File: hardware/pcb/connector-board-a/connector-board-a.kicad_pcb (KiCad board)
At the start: 2 copper layers, 27.4 x 39.1 mm, 22 parts, among them J1 DE9_Pins, J2 8-215570-0, Q3 2N7002, U4 TPS63001

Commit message: Routing of connector b board
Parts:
- J2: footprint TwinOak platform footprints:82155700 -> TwinOak:82155700
- JP1: value PWM -> PWM_MODE; footprint Jumper:SolderJumper-2_P1.3mm_Open_RoundedPad1.0x1.5mm -> Connector_PinHeader_2.54mm:PinHeader_1x02_P2.54mm_Vertical
- moved JP1 1.19 mm to (133.1, 107.2), turned to -90 degrees
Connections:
- net Net-(U4-PS/SYNC) renamed PS_SYNC
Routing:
- net I2C_SCL: track 26.7 -> 28.6 mm
- net VBAT_RAW: track 85.7 -> 87.3 mm, vias 2 -> 1
- net I2C_SDA: track 21.0 -> 21.8 mm
- net PS_SYNC: track 5.04 -> 5.76 mm

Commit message: Cleanup. Added feedback prevention circuits to Walter adapter
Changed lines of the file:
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@@
 		(pad "1" thru_hole rect
 			(at 0 0 180)
-			(size 1.3 1.3)
+			(size 1.3 1.8)
 			(drill 0.8)
 			(layers "*.Cu" "*.Mask")
@@
 			(pintype "passive")
 		)
-		(pad "2" thru_hole circle
+		(pad "2" thru_hole oval
 			(at 1.27 2.54 180)
-			(size 1.3 1.3)
+			(size 1.3 1.8)
 			(drill 0.8)
 			(layers "*.Cu" "*.Mask")
@@
 			(pinfunction "2_2")
 			(pintype "passive")
+			(thermal_bridge_angle 45)
 		)
 		(pad "3" thru_hole oval
 			(at 2.54 0 180)
-			(size 1.3 1.3)
+			(size 1.3 1.8)
 			(drill 0.8)
 			(layers "*.Cu" "*.Mask")
@@
 			(thermal_bridge_angle 45)
 		)
-		(pad "4" thru_hole circle
+		(pad "4" thru_hole oval
 			(at 3.81 2.54 180)
-			(size 1.3 1.3)
+			(size 1.3 1.8)
 			(drill 0.8)
 			(layers "*.Cu" "*.Mask")
@@
 			(pinfunction "4_4")
 			(pintype "passive")
+			(thermal_bridge_angle 45)
 		)
-		(pad "5" thru_hole circle
+		(pad "5" thru_hole oval
 			(at 5.08 0 180)
-			(size 1.3 1.3)
+			(size 1.3 1.8)
 			(drill 0.8)
 			(layers "*.Cu" "*.Mask")
@@
 			(pinfunction "5_5")
 			(pintype "passive")
+			(thermal_bridge_angle 45)
 		)
-		(pad "6" thru_hole circle
+		(pad "6" thru_hole oval
 			(at 6.35 2.54 180)
-			(size 1.3 1.3)
+			(size 1.3 1.8)
 			(drill 0.8)
 			(layers "*.Cu" "*.Mask")
@@
 			(pinfunction "6_6")
 			(pintype "passive")
+			(thermal_bridge_angle 45)
 		)
-		(pad "7" thru_hole circle
+		(pad "7" thru_hole oval
 			(at 7.62 0 180)
-			(size 1.3 1.3)
+			(size 1.3 1.8)
 			(drill 0.8)
 			(layers "*.Cu" "*.Mask")
@@
 			(pinfunction "7_7")
 			(pintype "passive")
+			(thermal_bridge_angle 45)
 		)
-		(pad "8" thru_hole circle
+		(pad "8" thru_hole oval
 			(at 8.89 2.54 180)
-			(size 1.3 1.3)
+			(size 1.3 1.8)
 			(drill 0.8)
 			(layers "*.Cu" "*.Mask")
@@
 			(pinfunction "8_8")
 			(pintype "passive")
+			(thermal_bridge_angle 45)
 		)
-		(pad "9" thru_hole circle
+		(pad "9" thru_hole oval
 			(at 10.16 0 180)
-			(size 1.3 1.3)
+			(size 1.3 1.8)
 			(drill 0.8)
 			(layers "*.Cu" "*.Mask")
@@
 			(pinfunction "9_9")
 			(pintype "passive")
+			(thermal_bridge_angle 45)
 		)
-		(pad "10" thru_hole circle
+		(pad "10" thru_hole oval
 			(at 11.43 2.54 180)
-			(size 1.3 1.3)
+			(size 1.3 1.8)
 			(drill 0.8)
 			(layers "*.Cu" "*.Mask")
@@
 			(pinfunction "10_10")
 			(pintype "passive")
+			(thermal_bridge_angle 45)
 		)
 		(embedded_fonts no)
@@
 		(start 131.572 98.806)
 		(end 130.328 97.562)
-		(width 0.254)
+		(width 0.508)
 		(layer "F.Cu")
 		(net "Net-(U4-L1)")
@@
 		(start 132.58 98.814)
 		(end 133.858 97.536)
-		(width 0.254)
+		(width 0.508)
 		(layer "F.Cu")
 		(net "Net-(U4-L2)")
@@
 	)
 	(segment
-		(start 143.866 100.228)
-		(end 143.256 100.838)
-		(width 0.254)
-		(layer "B.Cu")
-		(net "GND")
-	)
-	(segment
 		(start 134.112 85.344)
 		(end 132.334 85.344)
@@
 	)
 	(segment
-		(start 133.604 92.964)
-		(end 133.35 93.218)
+		(start 143.002 100.838)
+		(end 132.08 100.838)
 		(width 0.254)
 		(layer "B.Cu")
@@
 	)
 	(segment
-		(start 145.184 100.228)
-		(end 143.866 100.228)
+		(start 133.604 92.964)
+		(end 133.35 93.218)
 		(width 0.254)
 		(layer "B.Cu")
@@
 	)
 	(segment
-		(start 133.604 91.44)
-		(end 133.604 92.964)
+		(start 143.612 100.228)
+		(end 143.002 100.838)
 		(width 0.254)
 		(layer "B.Cu")
@@
 	)
 	(segment
-		(start 134.112 85.344)
-		(end 134.112 75.692)
+		(start 133.604 91.44)
+		(end 133.604 92.964)
 		(width 0.254)
 		(layer "B.Cu")
@@
 	)
 	(segment
-		(start 143.256 100.838)
-		(end 132.08 100.838)
+		(start 134.112 85.344)
+		(end 134.112 75.692)
 		(width 0.254)
 		(layer "B.Cu")
@@
 	)
 	(segment
+		(start 145.184 100.228)
+		(end 143.612 100.228)
+		(width 0.254)
+		(layer "B.Cu")
+		(net "GND")
+	)
+	(segment
 		(start 137.549 72.255)
 		(end 149.217 72.255)
@@
 		(start 131.196 91.44)
 		(end 131.196 93.122)
-		(width 0.254)
+		(width 0.508)
 		(layer "F.Cu")
 		(net "VBAT_RAW")
@@
 		(start 129.032 93.98)
 		(end 129.032 99.822)
-		(width 0.254)
+		(width 0.508)
 		(layer "F.Cu")
 		(net "VBAT_RAW")
@@
 		(start 131.292 93.218)
 		(end 129.794 93.218)
-		(width 0.254)
+		(width 0.508)
 		(layer "F.Cu")
 		(net "VBAT_RAW")
@@
 		(start 129.416 99.438)
 		(end 131.08 99.438)
-		(width 0.254)
+		(width 0.508)
 		(layer "F.Cu")
 		(net "VBAT_RAW")
@@
 		(start 129.794 93.218)
 		(end 129.032 93.98)
-		(width 0.254)
+		(width 0.508)
 		(layer "F.Cu")
 		(net "VBAT_RAW")
@@
 		(start 129.032 99.822)
 		(end 129.416 99.438)
-		(width 0.254)
+		(width 0.508)
 		(layer "F.Cu")
 		(net "VBAT_RAW")
@@
 		(start 129.032 104.648)
 		(end 129.032 99.314)
-		(width 0.254)
+		(width 0.508)
 		(layer "B.Cu")
 		(net "VBAT_RAW")
@@
 		(start 133.101 107.188)
 		(end 133.101 105.669)
-		(width 0.254)
+		(width 0.508)
 		(layer "B.Cu")
 		(net "VBAT_RAW")
@@
 		(start 132.588 105.156)
 		(end 129.54 105.156)
-		(width 0.254)
+		(width 0.508)
 		(layer "B.Cu")
 		(net "VBAT_RAW")
@@
 		(start 129.54 105.156)
 		(end 129.032 104.648)
-		(width 0.254)
+		(width 0.508)
 		(layer "B.Cu")
 		(net "VBAT_RAW")
@@
 		(start 133.101 105.669)
 		(end 132.588 105.156)
-		(width 0.254)
+		(width 0.508)
 		(layer "B.Cu")
 		(net "VBAT_RAW")

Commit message: Final PCB adjuments to rev 1.1
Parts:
- moved C16 7.92 mm to (127.0, 97.5), turned to 90 degrees
- moved C17 5.43 mm to (128.8, 97.5), turned to 90 degrees
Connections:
- J1 pad SH: (no net) -> GND
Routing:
- net GND: track 83.4 -> 93.5 mm, vias 12 -> 42
- net VBAT_RAW: track 87.3 -> 79.9 mm
- net Net-(Q3-D): track 17.5 -> 18.0 mm, vias 0 -> 2
- added copper zone on F.Cu, net GND

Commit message: Routed new BME280 addition to connector A
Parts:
- added C22: 100n, Capacitor_SMD:C_0603_1608Metric, F.Cu at (127.3, 77.2)
- added C23: 100n, Capacitor_SMD:C_0603_1608Metric, F.Cu at (128.0, 74.9)
- added J3: J_ENV, Connector_PinHeader_2.54mm:PinHeader_1x04_P2.54mm_Vertical, F.Cu at (128.0, 81.3)
- added U5: BME280, Package_LGA:Bosch_LGA-8_2.5x2.5mm_P0.65mm_ClockwisePinNumbering, F.Cu at (130.1, 77.5)
- moved Q3 1.97 mm to (129.0, 88.9)
- moved R13 1.97 mm to (134.3, 88.7)
- moved C18 1.97 mm to (132.3, 88.8)
- moved R12 1.95 mm to (134.4, 84.8)
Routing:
- net 3V3_LORA: track 25.1 -> 63.0 mm
- net GND: track 93.5 -> 68.6 mm, vias 42 -> 44
- net I2C_SDA: track 21.8 -> 44.7 mm, vias 0 -> 1
- net I2C_SCL: track 28.6 -> 38.2 mm, vias 0 -> 1
- net Net-(Q3-D): track 18.0 -> 16.1 mm
- net LORA_PWR_KILL: track 17.4 -> 19.3 mm
- net Net-(Q3-G): track 10.7 -> 9.13 mm

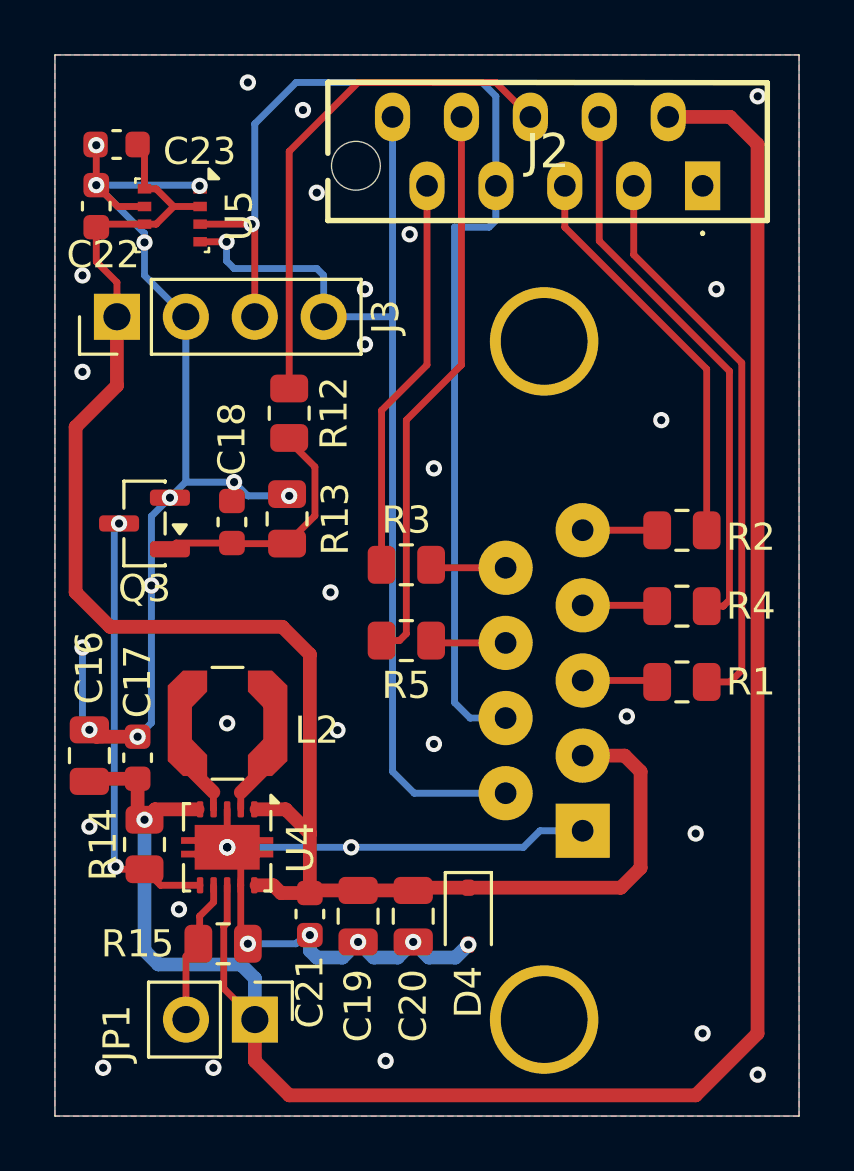
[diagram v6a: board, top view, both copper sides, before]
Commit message: Changed via placements to avoid solderwicking
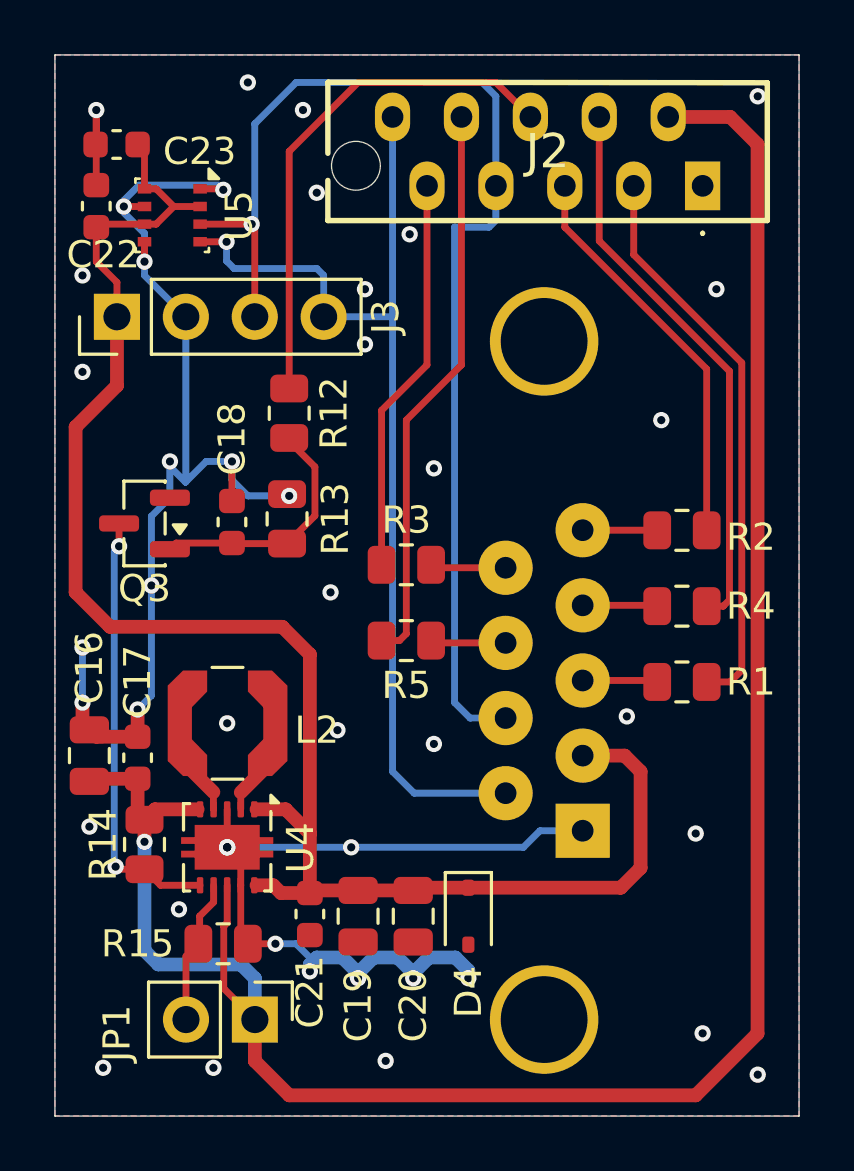
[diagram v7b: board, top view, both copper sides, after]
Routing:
- net GND: track 68.6 -> 74.8 mm

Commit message: Parts ordered!
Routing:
- net VBAT_RAW: track 79.9 -> 81.3 mm
- net Net-(Q3-D): track 16.1 -> 16.8 mm
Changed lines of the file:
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@@
 			)
 		)
-		(attr through_hole)
+		(attr through_hole exclude_from_pos_files exclude_from_bom)
 		(duplicate_pad_numbers_are_jumpers no)
 		(fp_line
@@
 	)
 	(segment
+		(start 134.2875 86.761)
+		(end 134.2875 87.818)
+		(width 0.254)
+		(layer "F.Cu")
+		(net "GND")
+	)
+	(segment
 		(start 127.254 74.904)
 		(end 127.228 74.93)
@@
 	)
 	(segment
-		(start 134.3 87.818)
-		(end 134.366 87.884)
-		(width 0.254)
-		(layer "F.Cu")
-		(net "GND")
-	)
-	(segment
 		(start 129.032 78.516)
 		(end 129.032 79.248)
@@
 	)
 	(segment
-		(start 134.2875 87.818)
-		(end 134.3 87.818)
-		(width 0.254)
-		(layer "F.Cu")
-		(net "GND")
-	)
-	(segment
 		(start 132.08 99.438)
 		(end 132.08 100.838)
@@
 	)
 	(via
-		(at 134.366 87.884)
+		(at 134.2875 86.761)
 		(size 0.6)
 		(drill 0.3)
@@
 	)
 	(via
-		(at 127 100.076)
-		(size 0.6)
-		(drill 0.3)
-		(layers "F.Cu" "B.Cu")
-		(free yes)
-		(net "GND")
-	)
-	(via
 		(at 127.254 73.66)
 		(size 0.6)
@@
 	)
 	(via
-		(at 132.08 100.838)
-		(size 0.6)
-		(drill 0.3)
-		(layers "F.Cu" "B.Cu")
-		(net "GND")
-	)
-	(via
 		(at 149.352 100.33)
 		(size 0.6)
@@
 	)
 	(via
+		(at 126.746 102.87)
+		(size 0.6)
+		(drill 0.3)
+		(layers "F.Cu" "B.Cu")
+		(free yes)
+		(net "GND")
+	)
+	(via
 		(at 137.16 82.296)
 		(size 0.6)
@@
 	(via
 		(at 131.572 108.966)
+		(size 0.6)
+		(drill 0.3)
+		(layers "F.Cu" "B.Cu")
+		(free yes)
+		(net "GND")
+	)
+	(via
+		(at 126.746 99.568)
 		(size 0.6)
 		(drill 0.3)
@@
 	)
 	(segment
+		(start 134.2875 86.761)
+		(end 134.1405 86.614)
+		(width 0.254)
+		(layer "B.Cu")
+		(net "GND")
+	)
+	(segment
 		(start 136.332 104.902)
 		(end 135.382 104.902)
@@
 	)
 	(segment
+		(start 134.1405 86.614)
+		(end 132.2555 86.614)
+		(width 0.254)
+		(layer "B.Cu")
+		(net "GND")
+	)
+	(segment
 		(start 128.27 76.988)
 		(end 128.83 76.428)
@@
 	)
 	(segment
-		(start 132.2555 87.2975)
-		(end 132.842 87.884)
-		(width 0.254)
-		(layer "B.Cu")
-		(net "GND")
-	)
-	(segment
 		(start 133.858 104.394)
 		(end 134.62 104.394)
@@
 	)
 	(segment
-		(start 132.842 87.884)
-		(end 134.366 87.884)
-		(width 0.254)
-		(layer "B.Cu")
-		(net "GND")
-	)
-	(segment
 		(start 138.938 105.476)
 		(end 138.364 104.902)
@@
 	)
 	(segment
-		(start 132.2555 86.614)
-		(end 132.2555 87.2975)
-		(width 0.254)
-		(layer "B.Cu")
-		(net "GND")
-	)
-	(segment
 		(start 145.184 100.228)
 		(end 143.612 100.228)
@@
 	)
 	(segment
-		(start 129.032 100.6345)
+		(start 129.032 99.946712)
 		(end 129.032 99.822)
+		(width 0.508)
+		(layer "F.Cu")
+		(net "VBAT_RAW")
+	)
+	(segment
+		(start 128.307106 100.671606)
+		(end 129.032 99.946712)
 		(width 0.508)
 		(layer "F.Cu")
@@
 	)
 	(segment
+		(start 127.881 100.671606)
+		(end 128.307106 100.671606)
+		(width 0.508)
+		(layer "F.Cu")
+		(net "VBAT_RAW")
+	)
+	(segment
 		(start 128.778 99.568)
 		(end 128.778 98.311)
@@
 	)
 	(via
-		(at 129.032 100.6345)
-		(size 0.6)
-		(drill 0.3)
-		(layers "F.Cu" "B.Cu")
+		(at 127.881 100.671606)
+		(size 0.6)
+		(drill 0.3)
+		(layers "F.Cu" "B.Cu")
+		(net "VBAT_RAW")
+	)
+	(segment
+		(start 129.54 105.156)
+		(end 132.588 105.156)
+		(width 0.508)
+		(layer "B.Cu")
 		(net "VBAT_RAW")
 	)
@@
 	)
 	(segment
-		(start 129.032 100.6345)
+		(start 127.881 100.671606)
+		(end 128.307106 100.671606)
+		(width 0.508)
+		(layer "B.Cu")
+		(net "VBAT_RAW")
+	)
+	(segment
+		(start 129.032 101.3965)
 		(end 129.032 104.648)
+		(width 0.508)
+		(layer "B.Cu")
+		(net "VBAT_RAW")
+	)
+	(segment
+		(start 128.307106 100.671606)
+		(end 129.032 101.3965)
 		(width 0.508)
 		(layer "B.Cu")
@@
 	)
 	(segment
-		(start 129.54 105.156)
-		(end 132.588 105.156)
-		(width 0.508)
-		(layer "B.Cu")
-		(net "VBAT_RAW")
-	)
-	(segment
 		(start 147.066 78.994)
 		(end 151.05 82.978)
@@
 	)
 	(segment
-		(start 135.3145 86.813)
-		(end 135.3145 88.616)
-		(width 0.254)
-		(layer "F.Cu")
-		(net "Net-(Q3-G)")
-	)
-	(segment
 		(start 132.2765 89.643)
 		(end 132.2555 89.622)
@@
 	)
 	(segment
+		(start 134.4035 85.786)
+		(end 135.3145 86.697)
+		(width 0.254)
+		(layer "F.Cu")
+		(net "Net-(Q3-G)")
+	)
+	(segment
 		(start 132.2555 89.622)
 		(end 130.1975 89.622)
@@
 	)
 	(segment
-		(start 134.2875 85.786)
-		(end 135.3145 86.813)
+		(start 135.3145 86.697)
+		(end 135.3145 88.616)
 		(width 0.254)
 		(layer "F.Cu")
@@
 	)
 	(segment
+		(start 134.2875 85.786)
+		(end 134.4035 85.786)
+		(width 0.254)
+		(layer "F.Cu")
+		(net "Net-(Q3-G)")
+	)
+	(segment
 		(start 147.9015 91.918)
 		(end 147.9315 91.948)
@@
 	)
 	(segment
-		(start 127.9675 101.5515)
-		(end 128.063 101.647)
-		(width 0.254)
-		(layer "F.Cu")
-		(net "Net-(Q3-D)")
-	)
-	(segment
-		(start 128.063 101.647)
-		(end 129.032 101.647)
+		(start 127.741983 101.459437)
+		(end 127.929546 101.647)
 		(width 0.254)
 		(layer "F.Cu")
@@
 	)
 	(segment
+		(start 127.929546 101.647)
+		(end 129.032 101.647)
+		(width 0.254)
+		(layer "F.Cu")
+		(net "Net-(Q3-D)")
+	)
+	(segment
 		(start 129.623 102.238)
 		(end 129.032 101.647)
@@
 	)
 	(via
-		(at 127.9675 101.5515)
+		(at 127.741983 101.459437)
 		(size 0.6)
 		(drill 0.3)
@@
 	)
 	(segment
-		(start 128.0945 89.7405)
+		(start 127.254 100.971454)
+		(end 127.254 100.33)
+		(width 0.254)
+		(layer "B.Cu")
+		(net "Net-(Q3-D)")
+	)
+	(segment
+		(start 127.919 89.916)
+		(end 128.0945 89.7405)
+		(width 0.254)
+		(layer "B.Cu")
+		(net "Net-(Q3-D)")
+	)
+	(segment
+		(start 127.254 100.33)
+		(end 127.919 99.665)
+		(width 0.254)
+		(layer "B.Cu")
+		(net "Net-(Q3-D)")
+	)
+	(segment
+		(start 127.741983 101.459437)
+		(end 127.254 100.971454)
+		(width 0.254)
+		(layer "B.Cu")
+		(net "Net-(Q3-D)")
+	)
+	(segment
+		(start 127.919 99.665)
 		(end 127.919 89.916)
 		(width 0.254)
 		(layer "B.Cu")
-		(net "Net-(Q3-D)")
-	)
-	(segment
-		(start 127.919 101.503)
-		(end 127.9675 101.5515)
-		(width 0.254)
-		(layer "B.Cu")
-		(net "Net-(Q3-D)")
-	)
-	(segment
-		(start 127.919 89.916)
-		(end 127.919 101.503)
-		(width 0.254)
-		(layer "B.Cu")
